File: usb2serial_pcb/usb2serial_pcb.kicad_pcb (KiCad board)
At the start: 2 copper layers, 22.4 x 16.6 mm, 29 parts, among them J1 USB_C_Receptacle_USB2.0, J2 DBUS, J3 UART1, J4 UART3, Q1 MMBT3904T, U1 XC6206P332MR, U2 STM32F103C8T6, Y1 Crystal_8M

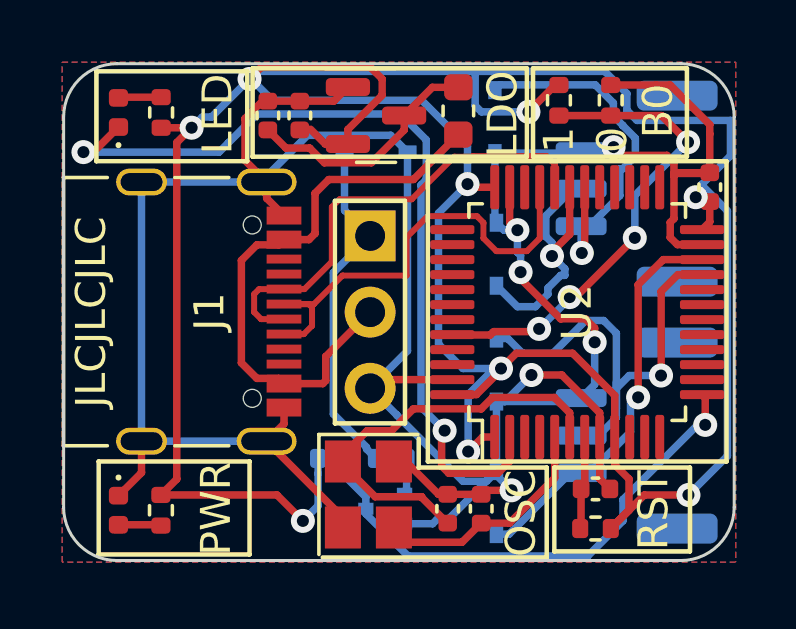
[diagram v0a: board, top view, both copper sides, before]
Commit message: add pull up register for USB enum
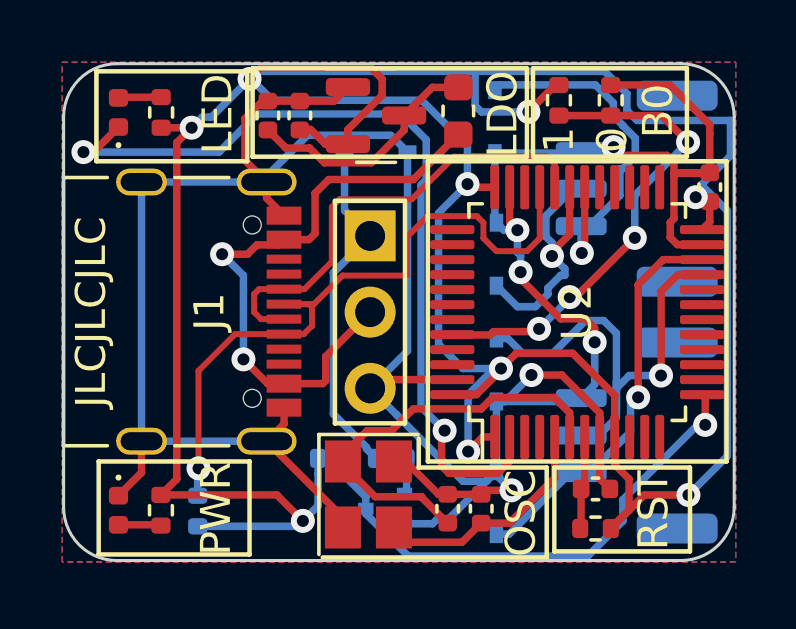
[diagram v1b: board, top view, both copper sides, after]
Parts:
- added R8: 1.5K, Resistor_SMD:R_0402_1005Metric, B.Cu at (52.6, 46.7)
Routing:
- net /USB_D+: track 15.8 -> 23.3 mm, vias 0 -> 1
- net +3.3V: track 106.7 -> 110.3 mm
- net +5V: track 19.2 -> 20.1 mm, vias 0 -> 2
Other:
- board text removed: "@GMaster"
- board text removed: "myaki"
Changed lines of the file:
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@@
   )
   (setup
+    (stackup
+      (layer "F.SilkS" (type "Top Silk Screen"))
+      (layer "F.Paste" (type "Top Solder Paste"))
+      (layer "F.Mask" (type "Top Solder Mask") (thickness 0.01))
+      (layer "F.Cu" (type "copper") (thickness 0.035))
+      (layer "dielectric 1" (type "core") (thickness 1.51) (material "FR4") (epsilon_r 4.5) (loss_tangent 0.02))
+      (layer "B.Cu" (type "copper") (thickness 0.035))
+      (layer "B.Mask" (type "Bottom Solder Mask") (thickness 0.01))
+      (layer "B.Paste" (type "Bottom Solder Paste"))
+      (layer "B.SilkS" (type "Bottom Silk Screen"))
+      (copper_finish "None")
+      (dielectric_constraints no)
+    )
     (pad_to_mask_clearance 0)
     (pcbplotparams
@@
       (outputformat 1)
       (mirror false)
-      (drillshape 1)
+      (drillshape 0)
       (scaleselection 1)
-      (outputdirectory "")
+      (outputdirectory "gerber")
     )
   )
@@
     )
   )
+  (footprint "Resistor_SMD:R_0402_1005Metric" (layer "B.Cu")
+    (at 52.6288 46.7106 90)
+    (descr "Resistor SMD 0402 (1005 Metric), square (rectangular) end terminal, IPC_7351 nominal, (Body size source: IPC-SM-782 page 72, https://www.pcb-3d.com/wordpress/wp-content/uploads/ipc-sm-782a_amendment_1_and_2.pdf), generated with kicad-footprint-generator")
+    (tags "resistor")
+    (property "Sheetfile" "usb2serial_pcb.kicad_sch")
+    (property "Sheetname" "")
+    (attr smd)
+    (fp_text reference "R8" (at 0 1.17 90) (layer "B.SilkS") hide
+      (effects (font (size 1 1) (thickness 0.15)) (justify mirror))
+    )
+    (fp_text value "1.5K" (at 0 -1.17 90) (layer "B.Fab") hide
+      (effects (font (size 1 1) (thickness 0.15)) (justify mirror))
+    )
+    (fp_text user "${REFERENCE}" (at 0 0 90) (layer "B.Fab")
+      (effects (font (size 0.26 0.26) (thickness 0.04)) (justify mirror))
+    )
+    (fp_line (start -0.153641 0.38) (end 0.153641 0.38) (layer "B.SilkS") (width 0.12))
+    (fp_line (start -0.153641 -0.38) (end 0.153641 -0.38) (layer "B.SilkS") (width 0.12))
+    (fp_line (start -0.93 -0.47) (end -0.93 0.47) (layer "B.CrtYd") (width 0.05))
+    (fp_line (start 0.93 -0.47) (end -0.93 -0.47) (layer "B.CrtYd") (width 0.05))
+    (fp_line (start -0.93 0.47) (end 0.93 0.47) (layer "B.CrtYd") (width 0.05))
+    (fp_line (start 0.93 0.47) (end 0.93 -0.47) (layer "B.CrtYd") (width 0.05))
+    (fp_line (start 0.525 0.27) (end 0.525 -0.27) (layer "B.Fab") (width 0.1))
+    (fp_line (start 0.525 -0.27) (end -0.525 -0.27) (layer "B.Fab") (width 0.1))
+    (fp_line (start -0.525 0.27) (end 0.525 0.27) (layer "B.Fab") (width 0.1))
+    (fp_line (start -0.525 -0.27) (end -0.525 0.27) (layer "B.Fab") (width 0.1))
+    (pad "1" smd roundrect (at -0.51 0 90) (size 0.54 0.64) (layers "B.Cu" "B.Paste" "B.Mask") (roundrect_rratio 0.25)
+      (net 1 "+3.3V") (pintype "passive"))
+    (pad "2" smd roundrect (at 0.51 0 90) (size 0.54 0.64) (layers "B.Cu" "B.Paste" "B.Mask") (roundrect_rratio 0.25)
+      (net 16 "/USB_D+") (pintype "passive"))
+    (model "${KICAD6_3DMODEL_DIR}/Resistor_SMD.3dshapes/R_0402_1005Metric.wrl"
+      (offset (xyz 0 0 0))
+      (scale (xyz 1 1 1))
+      (rotate (xyz 0 0 0))
+    )
+  )
   (footprint "Diode_SMD:D_SOD-323" (layer "B.Cu")
     (at 62.5348 33.7312 -90)
@@
     (effects (font (size 1 1) (thickness 0.15)) (justify mirror))
   )
-  (gr_text "myaki" (at 54.102 45.8724) (layer "B.SilkS")
-    (effects (font (size 1.3 1.3) (thickness 0.25)) (justify mirror))
-  )
   (gr_text "UART3" (at 60.96 44.196 90) (layer "B.SilkS")
     (effects (font (size 1 1) (thickness 0.15)) (justify mirror))
@@
   )
   (gr_text "T" (at 63.9572 37.3888) (layer "B.SilkS")
-    (effects (font (size 1 1) (thickness 0.15)) (justify mirror))
-  )
-  (gr_text "@GMaster" (at 52.5272 47.5996) (layer "B.SilkS")
     (effects (font (size 1 1) (thickness 0.15)) (justify mirror))
   )
@@
   (segment (start 63.6524 33.4057) (end 62.0843 33.4057) (width 0.25) (layer "B.Cu") (net 1))
   (segment (start 62.0843 33.4057) (end 61.8758 33.1972) (width 0.25) (layer "B.Cu") (net 1))
+  (segment (start 52.6288 47.2206) (end 55.9542 47.2206) (width 0.25) (layer "B.Cu") (net 1))
   (segment (start 60.6552 36.7792) (end 60.6552 41.148) (width 0.25) (layer "B.Cu") (net 1))
   (segment (start 66.9342 33.354573) (end 67.271027 33.6914) (width 0.25) (layer "B.Cu") (net 1))
@@
   (segment (start 61.468 41.9608) (end 62.738 41.9608) (width 0.25) (layer "B.Cu") (net 1))
   (segment (start 69.418614 36.060356) (end 69.418614 35.838986) (width 0.25) (layer "B.Cu") (net 1))
+  (segment (start 55.9542 47.2206) (end 56.134 47.0408) (width 0.25) (layer "B.Cu") (net 1))
   (segment (start 56.134 47.0408) (end 56.64 46.5348) (width 0.25) (layer "B.Cu") (net 1))
   (segment (start 69.418614 35.838986) (end 70.2842 36.704573) (width 0.25) (layer "B.Cu") (net 1))
@@
   (segment (start 54.61 33.4772) (end 53.6448 34.4424) (width 0.25) (layer "B.Cu") (net 13))
   (segment (start 59.3852 33.4772) (end 54.61 33.4772) (width 0.25) (layer "B.Cu") (net 13))
+  (segment (start 54.29002 38.1508) (end 53.4416 38.1508) (width 0.25) (layer "F.Cu") (net 14))
   (segment (start 56.79818 42.46502) (end 55.5058 42.46502) (width 0.25) (layer "F.Cu") (net 14))
-  (segment (start 54.0834 38.35742) (end 54.6008 37.84002) (width 0.25) (layer "F.Cu") (net 14))
-  (segment (start 55.3308 37.84002) (end 55.5058 37.66502) (width 0.25) (layer "F.Cu") (net 14))
   (segment (start 55.5058 37.66502) (end 56.3358 37.66502) (width 0.25) (layer "F.Cu") (net 14))
   (segment (start 58.3754 40.0812) (end 56.896 41.5606) (width 0.25) (layer "F.Cu") (net 14))
   (segment (start 56.5404 37.46042) (end 56.5404 36.1188) (width 0.25) (layer "F.Cu") (net 14))
-  (segment (start 54.6008 37.84002) (end 55.3308 37.84002) (width 0.25) (layer "F.Cu") (net 14))
   (segment (start 56.896 42.3672) (end 56.79818 42.46502) (width 0.25) (layer "F.Cu") (net 14))
   (segment (start 56.5404 36.1188) (end 56.9976 35.6616) (width 0.25) (layer "F.Cu") (net 14))
   (segment (start 59.8171 35.6616) (end 61.3156 34.1631) (width 0.25) (layer "F.Cu") (net 14))
-  (segment (start 54.6008 42.29002) (end 54.0834 41.77262) (width 0.25) (layer "F.Cu") (net 14))
-  (segment (start 55.3308 42.29002) (end 54.6008 42.29002) (width 0.25) (layer "F.Cu") (net 14))
+  (segment (start 55.3308 37.84002) (end 54.6008 37.84002) (width 0.25) (layer "F.Cu") (net 14))
+  (segment (start 54.6008 37.84002) (end 54.29002 38.1508) (width 0.25) (layer "F.Cu") (net 14))
+  (segment (start 55.5058 42.46502) (end 54.96182 42.46502) (width 0.25) (layer "F.Cu") (net 14))
+  (segment (start 54.96182 42.46502) (end 54.1528 41.656) (width 0.25) (layer "F.Cu") (net 14))
   (segment (start 56.3358 37.66502) (end 56.5404 37.46042) (width 0.25) (layer "F.Cu") (net 14))
   (segment (start 56.896 41.5606) (end 56.896 42.3672) (width 0.25) (layer "F.Cu") (net 14))
-  (segment (start 55.5058 42.46502) (end 55.3308 42.29002) (width 0.25) (layer "F.Cu") (net 14))
-  (segment (start 54.0834 41.77262) (end 54.0834 38.35742) (width 0.25) (layer "F.Cu") (net 14))
+  (segment (start 55.5058 37.66502) (end 55.3308 37.84002) (width 0.25) (layer "F.Cu") (net 14))
   (segment (start 56.9976 35.6616) (end 59.8171 35.6616) (width 0.25) (layer "F.Cu") (net 14))
+  (via (at 53.4416 38.1508) (size 0.8) (drill 0.4) (layers "F.Cu" "B.Cu") (net 14))
+  (via (at 54.1528 41.656) (size 0.8) (drill 0.4) (layers "F.Cu" "B.Cu") (net 14))
+  (segment (start 53.4416 38.1508) (end 54.1528 38.862) (width 0.25) (layer "B.Cu") (net 14))
+  (segment (start 54.1528 38.862) (end 54.1528 41.656) (width 0.25) (layer "B.Cu") (net 14))
   (segment (start 60.29767 36.8812) (end 59.5884 37.59047) (width 0.2) (layer "F.Cu") (net 16))
   (segment (start 59.5884 37.59047) (end 59.5884 38.862) (width 0.2) (layer "F.Cu") (net 16))
@@
   (segment (start 64.028 37.6228) (end 63.6016 38.0492) (width 0.2) (layer "F.Cu") (net 16))
   (segment (start 62.153 37.10087) (end 61.93333 36.8812) (width 0.2) (layer "F.Cu") (net 16))
+  (segment (start 53.87618 40.81502) (end 52.6553 42.0359) (width 0.2) (layer "F.Cu") (net 16))
   (segment (start 62.5856 38.0492) (end 62.153 37.6166) (width 0.2) (layer "F.Cu") (net 16))
+  (segment (start 52.6553 42.0359) (end 52.6553 45.2882) (width 0.2) (layer "F.Cu") (net 16))
   (segment (start 61.93333 36.8812) (end 60.29767 36.8812) (width 0.2) (layer "F.Cu") (net 16))
+  (segment (start 55.5058 40.81502) (end 53.87618 40.81502) (width 0.2) (layer "F.Cu") (net 16))
   (segment (start 63.6016 38.0492) (end 62.5856 38.0492) (width 0.2) (layer "F.Cu") (net 16))
   (segment (start 59.5884 38.862) (end 57.4548 38.862) (width 0.2) (layer "F.Cu") (net 16))
@@
   (segment (start 56.50178 39.81502) (end 55.5058 39.81502) (width 0.2) (layer "F.Cu") (net 16))
   (segment (start 57.4548 38.862) (end 56.50178 39.81502) (width 0.2) (layer "F.Cu") (net 16))
+  (via (at 52.6553 45.2882) (size 0.8) (drill 0.4) (layers "F.Cu" "B.Cu") (net 16))
+  (segment (start 52.6288 45.3147) (end 52.6553 45.2882) (width 0.25) (layer "B.Cu") (net 16))
+  (segment (start 52.6288 46.2006) (end 52.6288 45.3147) (width 0.25) (layer "B.Cu") (net 16))
   (segment (start 61.806123 34.8812) (end 61.786723 34.9006) (width 0.2) (layer "F.Cu") (net 17))
   (segment (start 57.3532 36.322) (end 57.0992 36.576) (width 0.2) (layer "F.Cu") (net 17))
